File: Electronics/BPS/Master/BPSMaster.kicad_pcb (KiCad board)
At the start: 2 copper layers, 100 x 75 mm, 186 parts, among them J1 SWD, J10 DisplayJumper, J11 FrontFans, J12 BackFans, J13 ErrorLightConnector, J2 Logic Analyzer, J20 USBConnector, J21 USB_B_Micro, J3 CurrentSlaveConnector, J4 CarPowerConnector, J5 CAN_Out, J6 ContactorConnector, J7 VoltageSlaveConnector, J8 DisplayConnector, J9 TempSlaveConnector, Q1 VND5N07-E, Q2 NVR4003NT3G, Q3 NVR4003NT3G, Q4 NVR4003NT3G, SW1 B3SL-1002P, U1 STM32F413RHTx, U10 LTC6820, U11 HX1188FNL, U12 LTC6820, U13 Si8641EC-B-IS1, U14 SI8660EC-B-IS1, U15 RI3-1205S, U16 SI8261ABC-IS, U17 CP2102N-A01-GQFN24, U2 RI3-1205S, U3 NCP1117-3.3_SOT223, U4 CDSOT23-T24CAN, U5 ADM3055E, U6 BAS70-04, U7 SI8261ABC-IS, U8 M24128, Y1 NX8045GB-8.000M-STD-CSJ-1

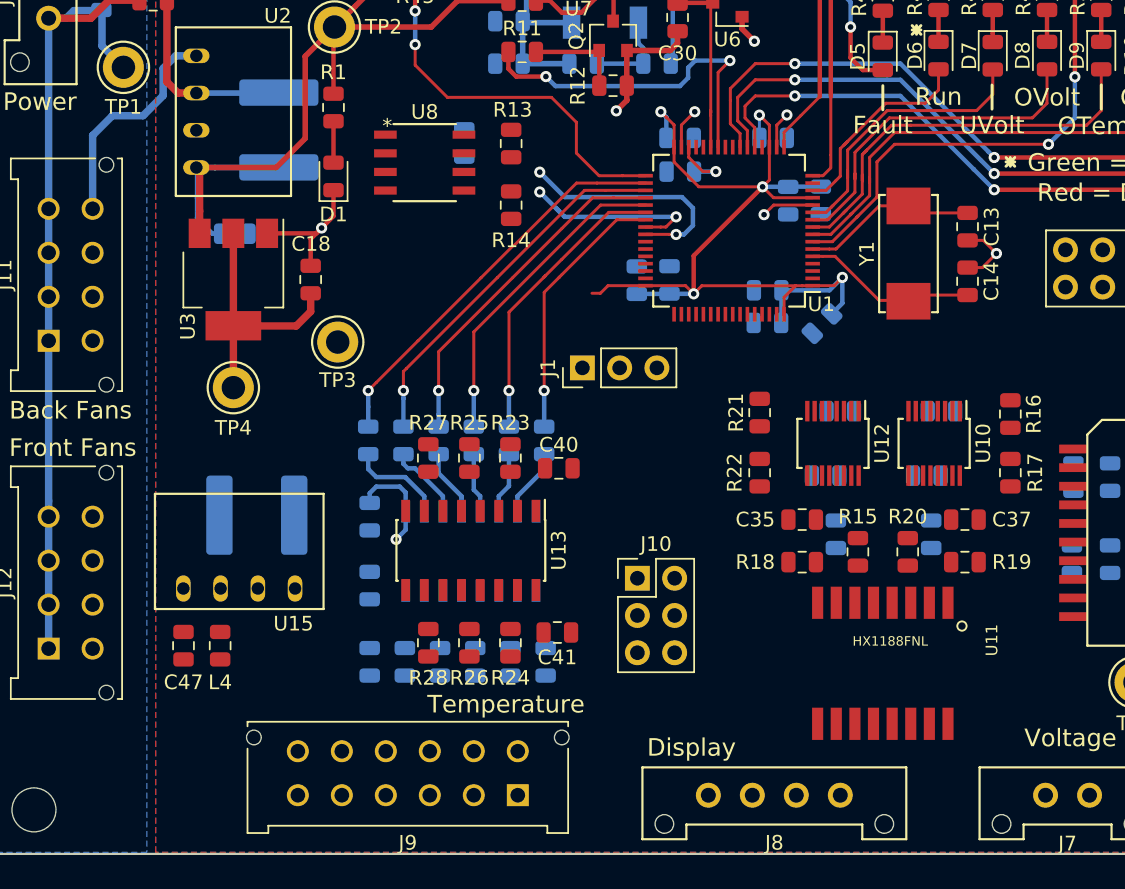
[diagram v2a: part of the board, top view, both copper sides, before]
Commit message: Added more traces to master BPS.
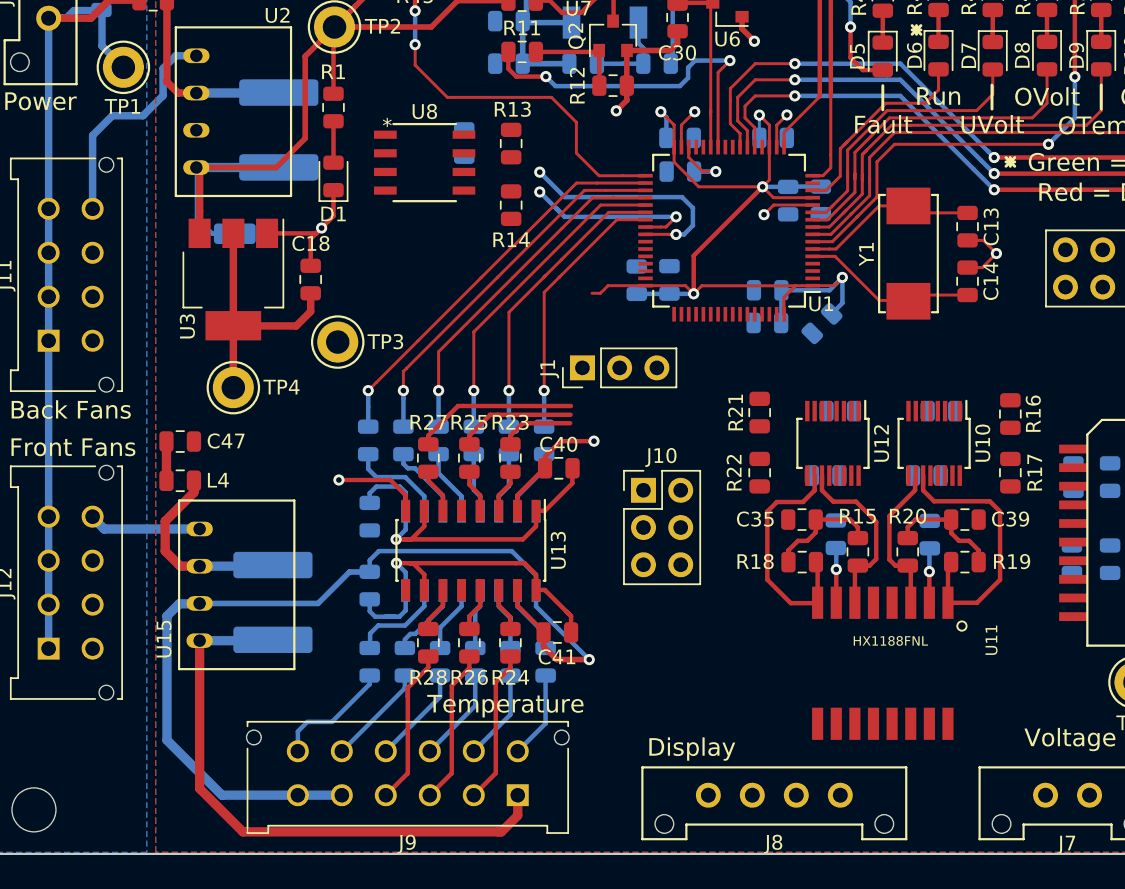
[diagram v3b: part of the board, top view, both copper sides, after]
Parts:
- C37: moved to B.Cu
- C39: moved to F.Cu
- moved C47 13.9 mm to (113.0, 121.9), turned to 0 degrees
- moved L4 11.6 mm to (113.0, 124.5), turned to 0 degrees
- moved C46 6.05 mm to (119.3, 132.8), turned to 270 degrees
- moved J10 6.01 mm to (144.6, 125.2)
- moved U15 2.71 mm to (114.3, 131.7), turned to 270 degrees
- moved C37 2.61 mm to (164.1, 128.2), turned to 90 degrees
- moved C39 2.51 mm to (166.5, 127.2), turned to 0 degrees
- turned C35 to 180 degrees
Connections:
- J9 pad 10: /SPI/CONN10 -> /SPI/CS3
- J9 pad 11: /SPI/CONN11 -> /SPI/CS2
- J9 pad 12: /SPI/CONN12 -> /SPI/CS1
- J9 pad 7: /SPI/CONN7 -> /SPI/CS6
- J9 pad 8: /SPI/CONN8 -> /SPI/CS5
- J9 pad 9: /SPI/CONN9 -> /SPI/CS4
- R30 pad 1: /SPI/CONN7 -> /SPI/CS1
- R32 pad 1: /SPI/CONN8 -> /SPI/CS2
- R34 pad 1: /SPI/CONN9 -> /SPI/CS3
- R36 pad 1: /SPI/CONN10 -> /SPI/CS4
- R38 pad 1: /SPI/CONN11 -> /SPI/CS5
- R40 pad 1: /SPI/CONN12 -> /SPI/CS6
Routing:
- net +5VL: track 0.00 -> 65.8 mm, vias 0 -> 1
- net GND_A: track 0.00 -> 65.4 mm, vias 0 -> 1
- net /SPI/VOLT_IP: track 0.00 -> 18.6 mm
- net +5V: track 106.3 -> 124.4 mm
- net /SPI/DISP_IM: track 0.00 -> 16.4 mm
- net GND: track 98.9 -> 113.2 mm, vias 10 -> 12
- net Net-(C46-Pad1): track 0.00 -> 13.4 mm
- net /SPI/DISP_IP: track 0.00 -> 12.2 mm
- net /SPI1_MISO: track 0.00 -> 11.2 mm
- net Net-(J9-Pad4): track 0.00 -> 11.0 mm
- net Net-(J9-Pad3): track 0.00 -> 10.6 mm
- net /SPI/VOLT_IM: track 0.00 -> 10.5 mm
- net Net-(J9-Pad2): track 0.00 -> 10.5 mm
- net /SPI/CS1: track 0.00 -> 8.17 mm
- net /SPI1_MOSI: track 0.00 -> 8.08 mm
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
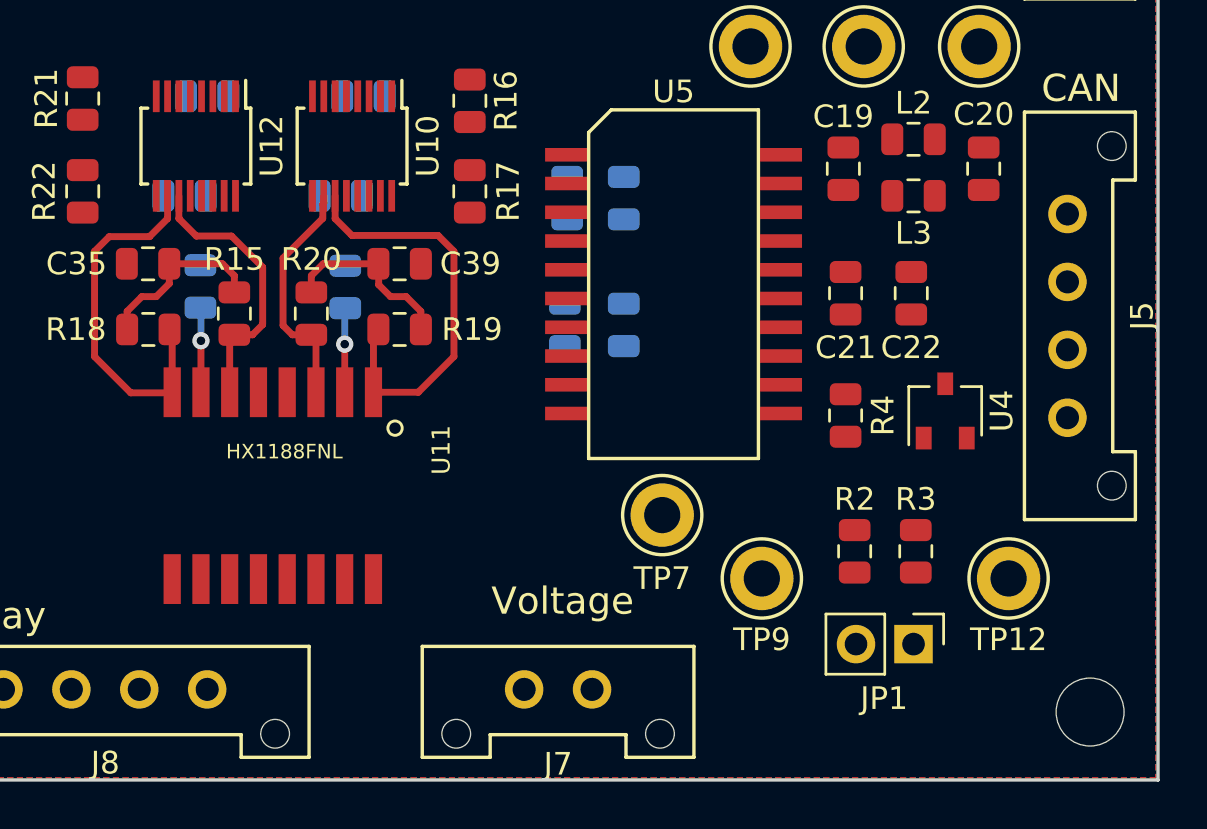
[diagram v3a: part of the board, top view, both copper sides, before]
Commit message: Routed CAN bus.
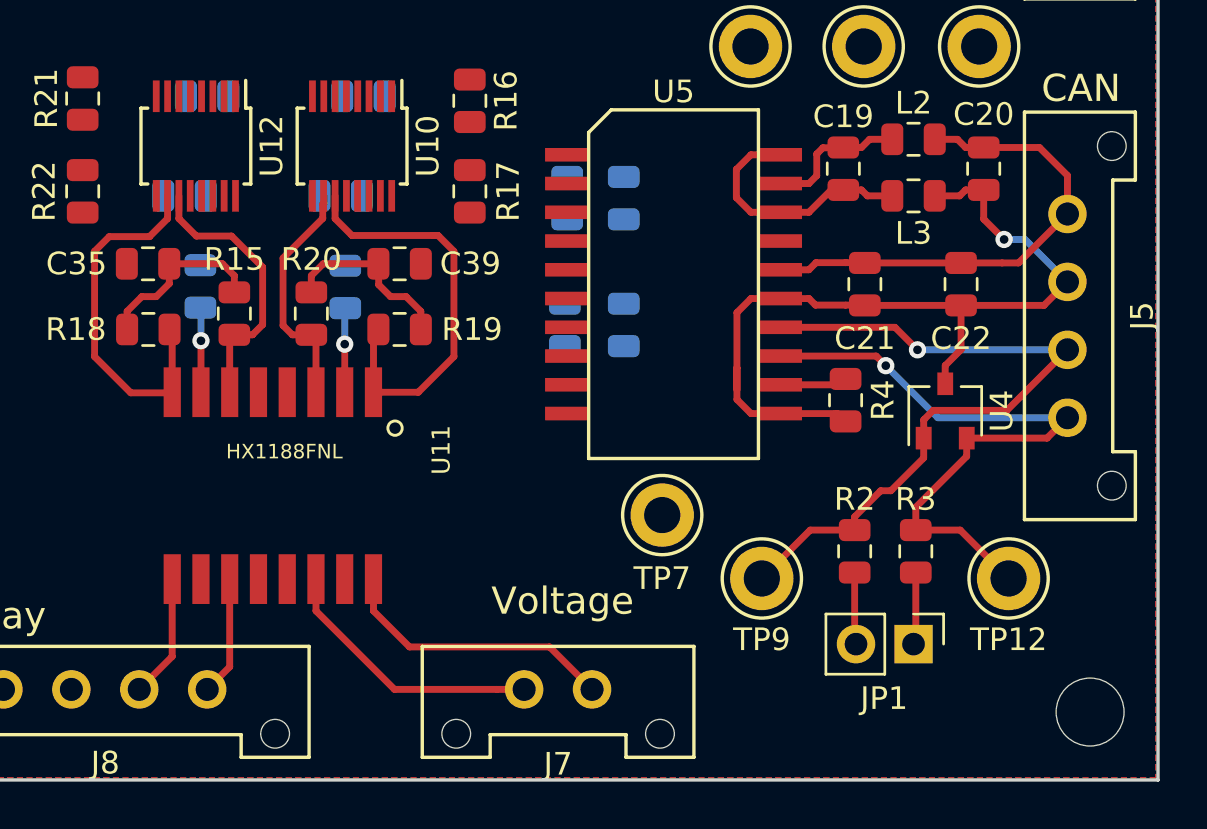
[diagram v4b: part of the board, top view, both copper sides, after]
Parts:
- moved C22 2.24 mm to (191.3, 128.1)
- moved C21 0.94 mm to (187.1, 128.1)
- moved R4 0.68 mm to (186.2, 133.2)
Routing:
- net Net-(C20-Pad2): track 0.00 -> 37.6 mm, vias 0 -> 1
- net /CAN/CAN_H: track 0.00 -> 32.1 mm, vias 0 -> 1
- net /CAN/CAN_L: track 0.00 -> 28.6 mm, vias 0 -> 1
- net Net-(C20-Pad1): track 0.00 -> 22.0 mm
- net Net-(J7-Pad1): track 0.00 -> 12.5 mm
- net Net-(J7-Pad2): track 0.00 -> 12.0 mm
- net Net-(C19-Pad2): track 0.00 -> 11.1 mm
- net Net-(C19-Pad1): track 0.00 -> 6.34 mm
- net Net-(J8-Pad2): track 0.00 -> 5.48 mm
- net Net-(J8-Pad1): track 0.00 -> 5.28 mm
- net /CAN/TERM_L: track 0.00 -> 3.20 mm
- net /CAN/TERM_H: track 0.00 -> 3.19 mm
- net /CAN/RSlope: track 0.00 -> 3.01 mm

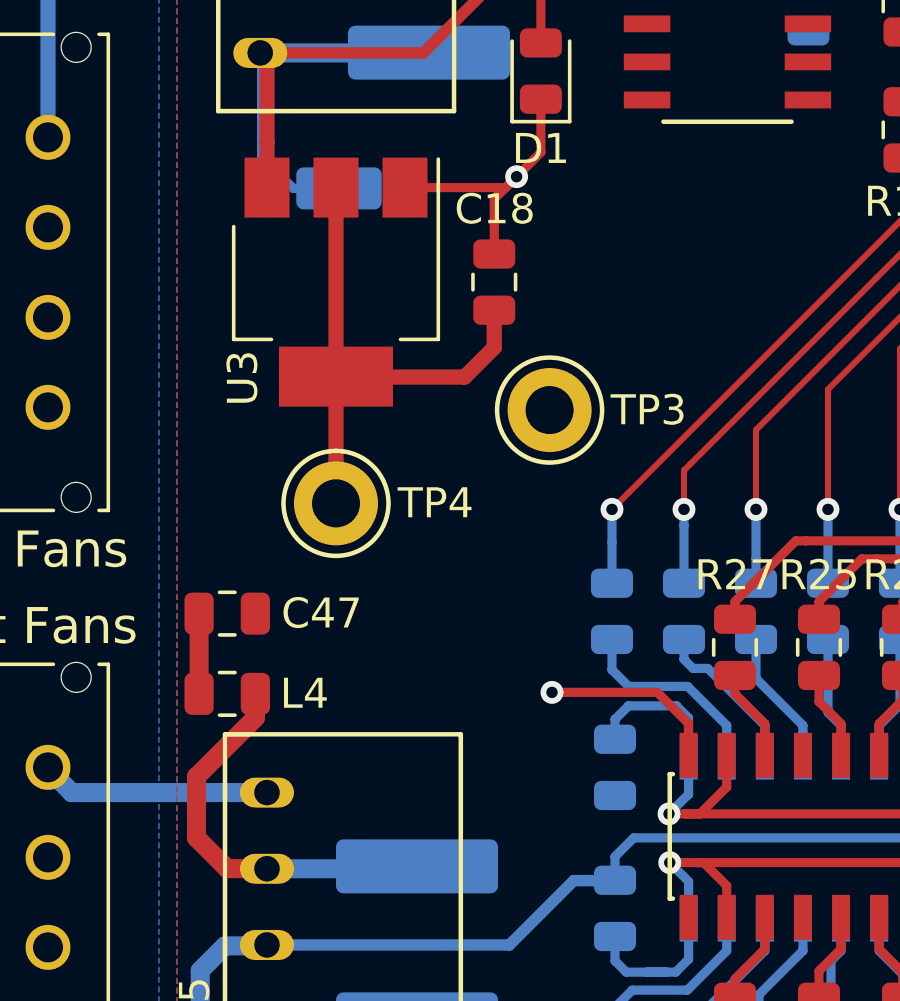
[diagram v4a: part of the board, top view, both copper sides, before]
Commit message: Added CAN bus traces on BPS.
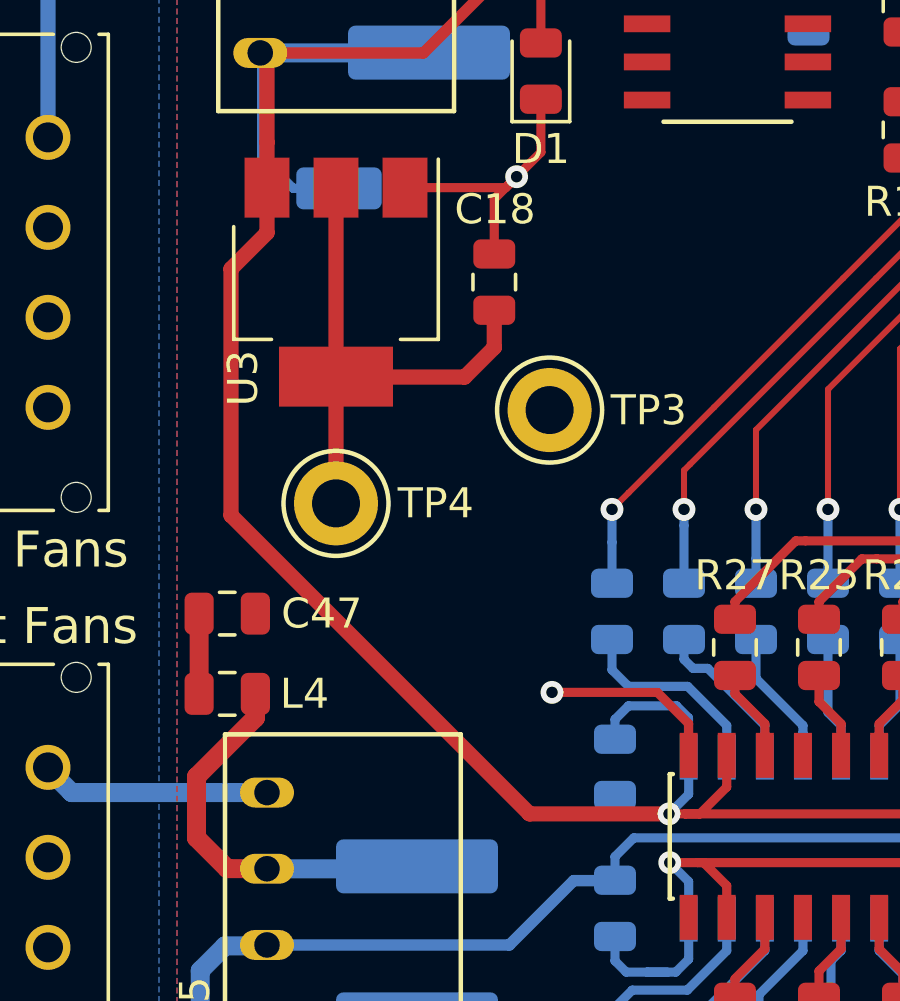
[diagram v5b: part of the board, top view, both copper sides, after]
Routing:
- net +5V: track 124.4 -> 154.5 mm
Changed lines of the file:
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@@
     (thickness 1.6)
     (drawings 96)
-    (tracks 1022)
+    (tracks 1027)
     (zones 0)
     (modules 186)
@@
   (segment (start 137.245 127.6548) (end 136.3498 128.55) (width 0.3048) (layer F.Cu) (net 5))
   (segment (start 137.245 126.6) (end 137.245 127.6548) (width 0.3048) (layer F.Cu) (net 5))
+  (segment (start 114.3 109.183) (end 113.1 110.383) (width 0.508) (layer F.Cu) (net 5))
+  (segment (start 114.3 107.675) (end 114.3 109.183) (width 0.508) (layer F.Cu) (net 5))
+  (segment (start 113.1 110.383) (end 113.1 118.6) (width 0.508) (layer F.Cu) (net 5))
+  (segment (start 123.05 128.55) (end 127.7 128.55) (width 0.508) (layer F.Cu) (net 5))
+  (segment (start 113.1 118.6) (end 123.05 128.55) (width 0.508) (layer F.Cu) (net 5))
   (segment (start 163.12931 106.27931) (end 162.65 105.8) (width 0.2032) (layer F.Cu) (net 6))
   (segment (start 166.680376 106.27931) (end 163.12931 106.27931) (width 0.2032) (layer F.Cu) (net 6))
@@
     (connect_pads (clearance 0.508))
     (min_thickness 0.254)
-    (fill yes (arc_segments 16) (thermal_gap 0.508) (thermal_bridge_width 0.508))
+    (fill (arc_segments 16) (thermal_gap 0.508) (thermal_bridge_width 0.508))
     (polygon
       (pts
@@
     (connect_pads (clearance 0.508))
     (min_thickness 0.254)
-    (fill yes (arc_segments 16) (thermal_gap 0.508) (thermal_bridge_width 0.508))
+    (fill (arc_segments 16) (thermal_gap 0.508) (thermal_bridge_width 0.508))
     (polygon
       (pts
@@
     (connect_pads (clearance 0.508))
     (min_thickness 0.254)
-    (fill yes (arc_segments 16) (thermal_gap 0.508) (thermal_bridge_width 0.508))
+    (fill (arc_segments 16) (thermal_gap 0.508) (thermal_bridge_width 0.508))
     (polygon
       (pts

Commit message: Completed master board PCB
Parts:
- removed C51: 4.7uF, Capacitor_SMD:C_0805_2012Metric
- removed C52: 0.1uF, Capacitor_SMD:C_0805_2012Metric
- removed D14: SP0503BAHT, Package_TO_SOT_SMD:SOT-143
- removed J20: USBConnector, UTSVT_Connectors:Molex_MicroFit3.0_1x4xP3.00mm_PolarizingPeg_Vertical
- removed J21: USB_B_Micro, Connector_USB:USB_Micro-B_Molex-105017-0001
- removed R55: 22.1k, Resistor_SMD:R_0805_2012Metric
- removed R56: 47.5k, Resistor_SMD:R_0805_2012Metric
- removed R59: 1k, Resistor_SMD:R_0805_2012Metric
- removed U17: CP2102N-A01-GQFN24, Package_DFN_QFN:QFN-24-1EP_4x4mm_P0.5mm_EP2.6x2.6mm
- added J14: Conn_01x03, Connector_PinHeader_2.54mm:PinHeader_1x02_P2.54mm_Vertical, F.Cu at (127.6, 108.4)
- J2: footprint Connector_PinHeader_2.54mm:PinHeader_2x07_P2.54mm_Vertical -> Connector_PinHeader_2.54mm:PinHeader_2x05_P2.54mm_Vertical
- moved C42 7.94 mm to (150.2, 121.5), turned to 90 degrees
- moved R21 5.60 mm to (158.1, 119.6)
- moved R22 5.60 mm to (158.1, 123.7)
- moved U12 5.05 mm to (152.4, 122.0), turned to 0 degrees
- moved C38 2.89 mm to (154.7, 122.5), turned to 90 degrees
- moved J10 2.87 mm to (145.0, 128.0)
- moved J2 1.72 mm to (186.9, 108.5)
- moved TP6 0.74 mm to (191.4, 117.6)
- moved TP7 0.73 mm to (178.5, 138.9)
- moved TP8 0.60 mm to (181.4, 117.6)
- moved C13 0.42 mm to (166.3, 107.2)
- moved C14 0.42 mm to (166.3, 110.9)
- moved R16 0.29 mm to (169.6, 119.7)
- moved R17 0.29 mm to (169.6, 123.7)
- turned D3 to 0 degrees
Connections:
- J2 pad 10: /CAN1_RX -> /SPI1_MOSI
- J2 pad 2: /SPI1_CLK -> /CAN1_TX
- J2 pad 3: /SPI1_MISO -> /UART1_TX
- J2 pad 4: /SPI1_MOSI -> /CAN1_RX
- J2 pad 5: /LTC6811_CS -> /UART1_RX
- J2 pad 6: /DISPLAY_CS -> /SPI1_CLK
- J2 pad 8: /I2C3_SDA -> /SPI1_MISO
- J2 pad 9: /I2C3_SCL -> Net-(J2-Pad9)
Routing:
- net +3V3: track 87.4 -> 215.0 mm, vias 5 -> 13
- net +12V: track 135.8 -> 221.8 mm, vias 2 -> 4
- net +5V: track 154.5 -> 233.9 mm, vias 3 -> 7
- net GNDPWR: track 94.5 -> 158.2 mm, vias 2 -> 3
- net /SPI1_MISO: track 11.2 -> 71.9 mm, vias 0 -> 5
- net /SPI1_CLK: track 5.01 -> 63.6 mm, vias 0 -> 4
- net /SPI1_MOSI: track 8.08 -> 64.2 mm, vias 0 -> 4
- net /CAN1_TX: track 0.00 -> 55.2 mm, vias 0 -> 2
- net GND: track 113.2 -> 162.9 mm, vias 12 -> 25
- net /CAN1_RX: track 0.00 -> 49.5 mm, vias 0 -> 2
- net /UART1_TX: track 0.00 -> 48.0 mm, vias 0 -> 2
- net /UART1_RX: track 0.00 -> 42.2 mm, vias 0 -> 2
- net /LTC6811_CS: track 0.00 -> 22.8 mm, vias 0 -> 2
- net +5VL: track 65.8 -> 80.9 mm
- net /DISPLAY_CS: track 0.00 -> 13.1 mm, vias 0 -> 2
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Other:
- board text added: "+3.3V"
- board text added: "0"
- board text added: "CLK"
- board text added: "CRX"
- board text added: "CTX"
- board text added: "Display SPI settings"
- board text added: "Gin"
- board text added: "Gout"
- board text added: "PHA"
- board text added: "POL"
- board text added: "SCL"
- board text added: "SDA"
- board text added: "Spring 2019: Monolo Alvarez Chase Block Corbin Capo Richard Li Garrett Wong Sijin Woo"
- board text added: "URX"
- board text added: "UTSVT - BPS Master v1.0 Spring 2019"
- board text added: "UTX"
- board text added: "Vin"
- board text added: "Vout"
- board text removed: "D+"
- board text removed: "D-"
- board text removed: "Green = Alive"
- board text removed: "USB"
- board text removed: "VBus"
